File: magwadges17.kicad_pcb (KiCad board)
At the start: 2 copper layers, 156 x 89.8 mm, 44 parts, among them J1 PGM, J2 JACK_2P, U1 ATTINY861A-SU

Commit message: Update center spinner
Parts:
- removed Gsp: LOGO, custom:spiral_pattern_large4
- added REF**: Centertouch, centerspin:centerspin, F.Cu at (150.0, 100.0)
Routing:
- net TouchC: track 2.57 -> 45.0 mm
- net TouchA: track 2.39 -> 42.7 mm
- net TouchB: track 2.44 -> 9.18 mm

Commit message: Update wadges
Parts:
- moved BT1 3.30 mm to (212.1, 89.2)
- moved J2 1.56 mm to (83.5, 97.2)
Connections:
- J1 pad 3: Net-(J1-Pad3) -> SW_F
- LS1 pad 2: Net-(J1-Pad3) -> Net-(LS1-Pad2)
- U1 pad 3: Net-(J1-Pad3) -> SW_F
- U1 pad 4: Net-(J2-Pad2) -> SW_G
- U1 pad 7: SW_F -> Net-(LS1-Pad2)
- U1 pad 8: SW_G -> Net-(J2-Pad2)
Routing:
- net Net-(LS1-Pad2): track 0.00 -> 110.1 mm
- net Net-(J1-Pad3): track 85.9 -> 0.00 mm
- net GND: track 323.4 -> 371.3 mm
- net SW_F: track 72.9 -> 85.7 mm
- net SW_G: track 67.0 -> 75.3 mm
- net Net-(J2-Pad2): track 99.5 -> 106.3 mm
- net VCC: track 127.7 -> 134.3 mm
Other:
- board text added: "GO"
- board text added: "GOTTA"
- board text added: "MAGWEST"
- board text added: "WEST"

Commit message: Update design
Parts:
- added D1: LED, SM0805, F.Cu at (186.5, 114.9)
- added D2: LED, SM0805, F.Cu at (113.4, 115.2)
- added D3: LED, SM0805, F.Cu at (113.5, 83.6)
- added D4: LED, SM0805, F.Cu at (185.5, 83.8)
- added L1: LANYARD, Connectors:1pin, F.Cu at (149.9, 63.2)
- added RN2: 10k, NETWORK1206, F.Cu at (163.6, 133.8)
- RN1: value R_Pack04 -> 1M
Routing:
- net Net-(D1-Pad2): track 33.0 -> 184.9 mm, vias 0 -> 10
- net Net-(D3-Pad1): track 0.00 -> 81.2 mm, vias 0 -> 6
- net Net-(D3-Pad2): track 22.9 -> 102.9 mm, vias 0 -> 4
- net Net-(D4-Pad1): track 0.00 -> 62.2 mm, vias 0 -> 4
- net Net-(D2-Pad1): track 0.00 -> 61.4 mm
- net Net-(D1-Pad1): track 0.00 -> 34.6 mm
- net GND: track 371.3 -> 396.3 mm, vias 0 -> 8
- net reset: track 21.4 -> 36.4 mm, vias 0 -> 2
- added copper zone on B.Cu, net GND
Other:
- outline, holes or cut-outs redrawn
- rule pad_to_mask_clearance: 0.2 -> 0.1
- board text removed: "GO"
- board text removed: "GOTTA"
- board text removed: "MAGWEST"
- board text removed: "WEST"

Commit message: Update with halftone
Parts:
- added ?: , halftone:halftone, B.Cu at (150.0, 100.0)
- moved RN2 23.1 mm to (181.4, 119.2)
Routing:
- net Net-(D1-Pad1): track 34.6 -> 4.81 mm
- net Net-(D3-Pad1): track 81.2 -> 102.1 mm
- net Net-(D2-Pad1): track 61.4 -> 74.1 mm
- net Net-(D4-Pad1): track 62.2 -> 49.5 mm, vias 4 -> 2
- net GND: track 396.3 -> 406.1 mm, vias 8 -> 9
- net Net-(D1-Pad2): track 184.9 -> 183.4 mm
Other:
- outline, holes or cut-outs redrawn

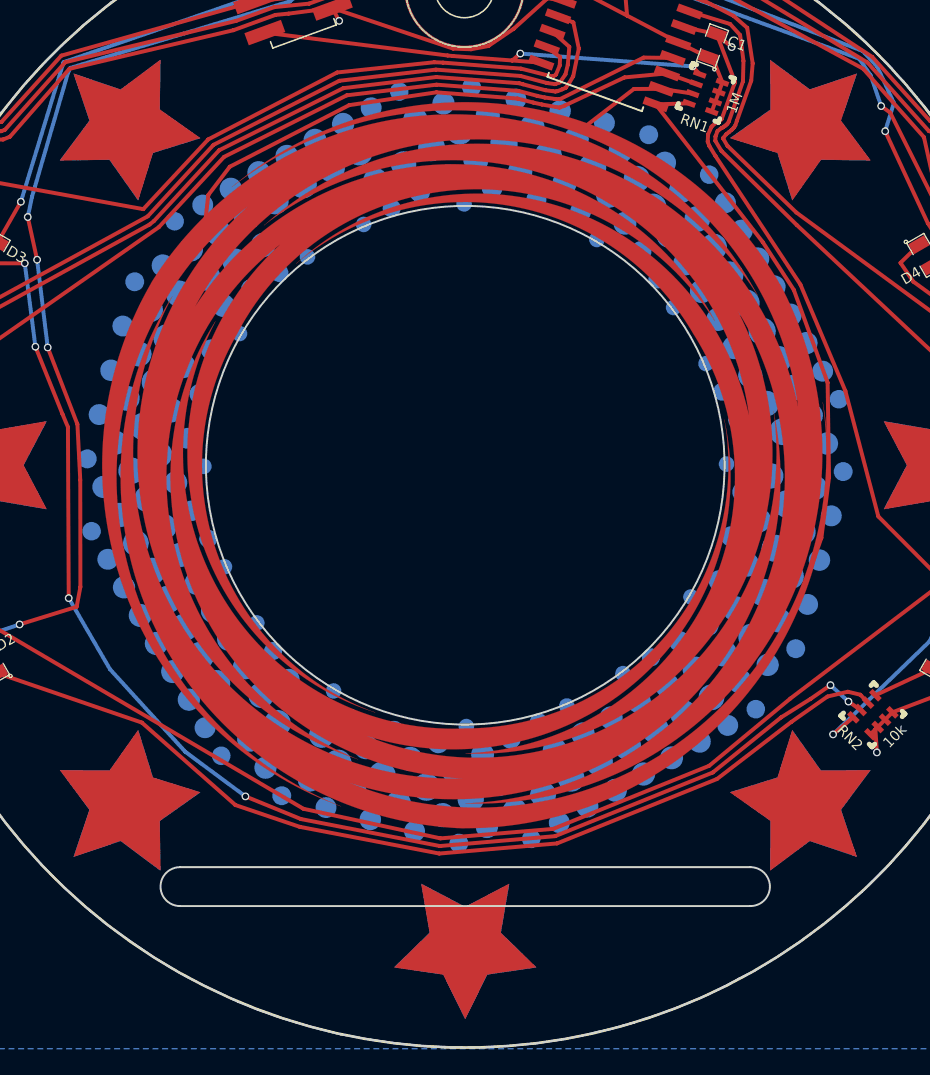
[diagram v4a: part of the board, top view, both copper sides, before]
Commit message: Update design with halftone, etc.
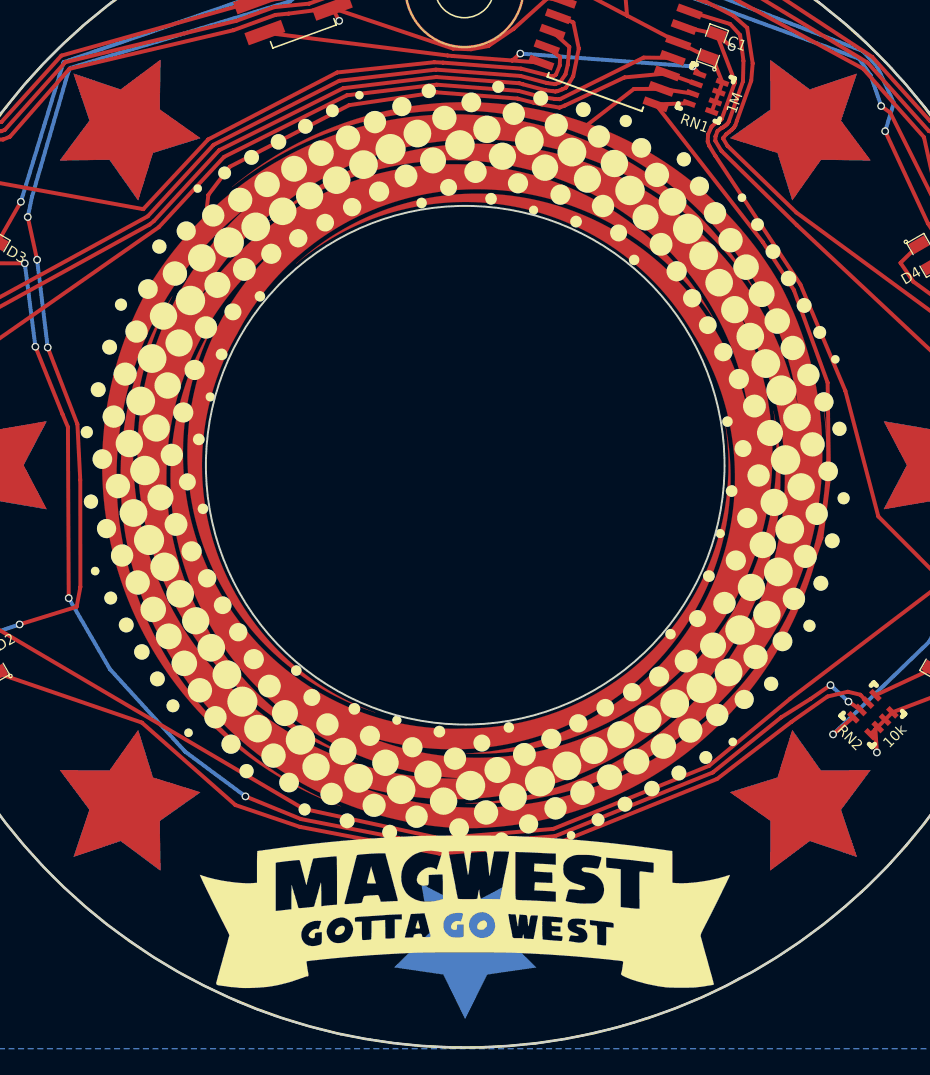
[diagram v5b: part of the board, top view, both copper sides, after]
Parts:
- removed G10, G3: LOGO, custom:test_star4
- removed G17, G24: LOGO, custom:test_star4_copper
- added ?: , halftone:halftoneSilk, F.Cu at (150.0, 100.0)
- added G***: LOGO, customs:Logo, F.Cu at (150.0, 135.5)
- added G18: LOGO, custom:test_star4_copper, B.Cu at (150.0, 137.5)
- added G4: LOGO, custom:test_star4, B.Cu at (150.0, 137.5)
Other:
- outline, holes or cut-outs redrawn

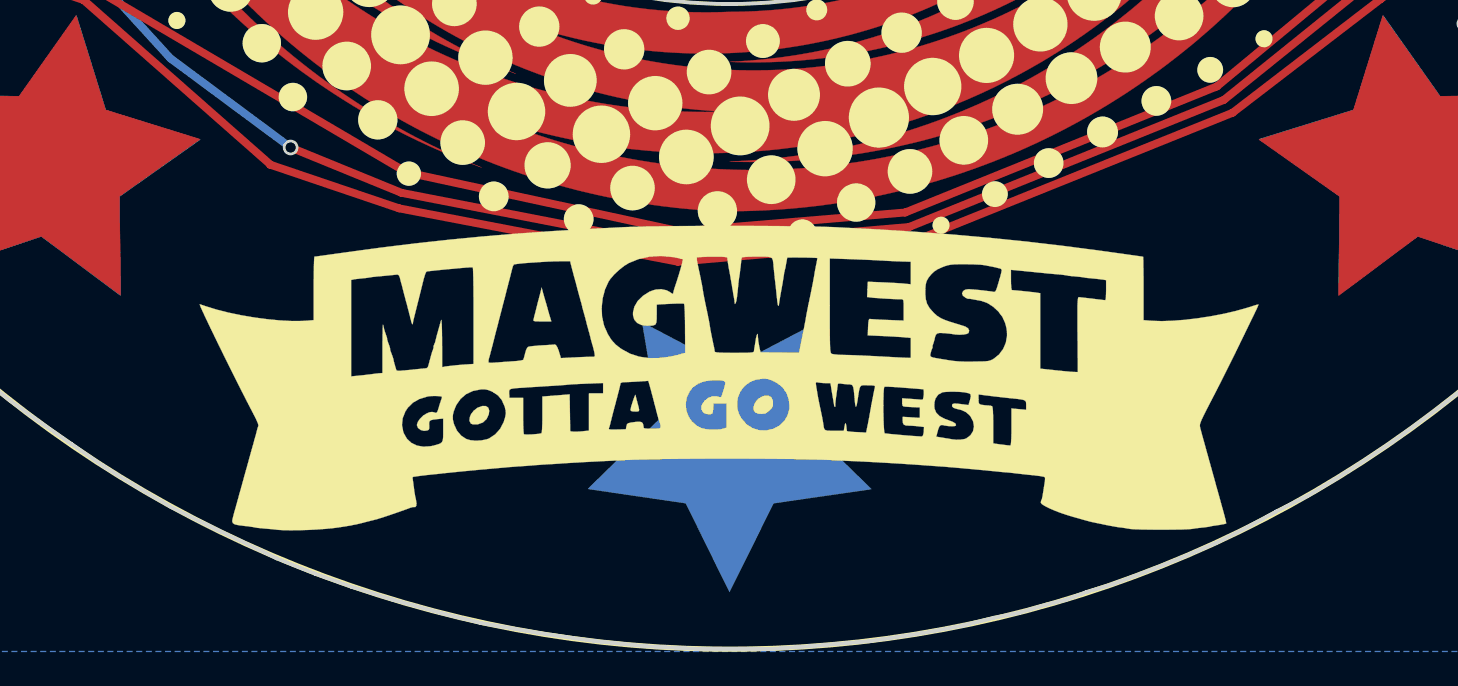
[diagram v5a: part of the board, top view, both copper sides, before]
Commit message: err apparently forgot tos ave acutal pcb
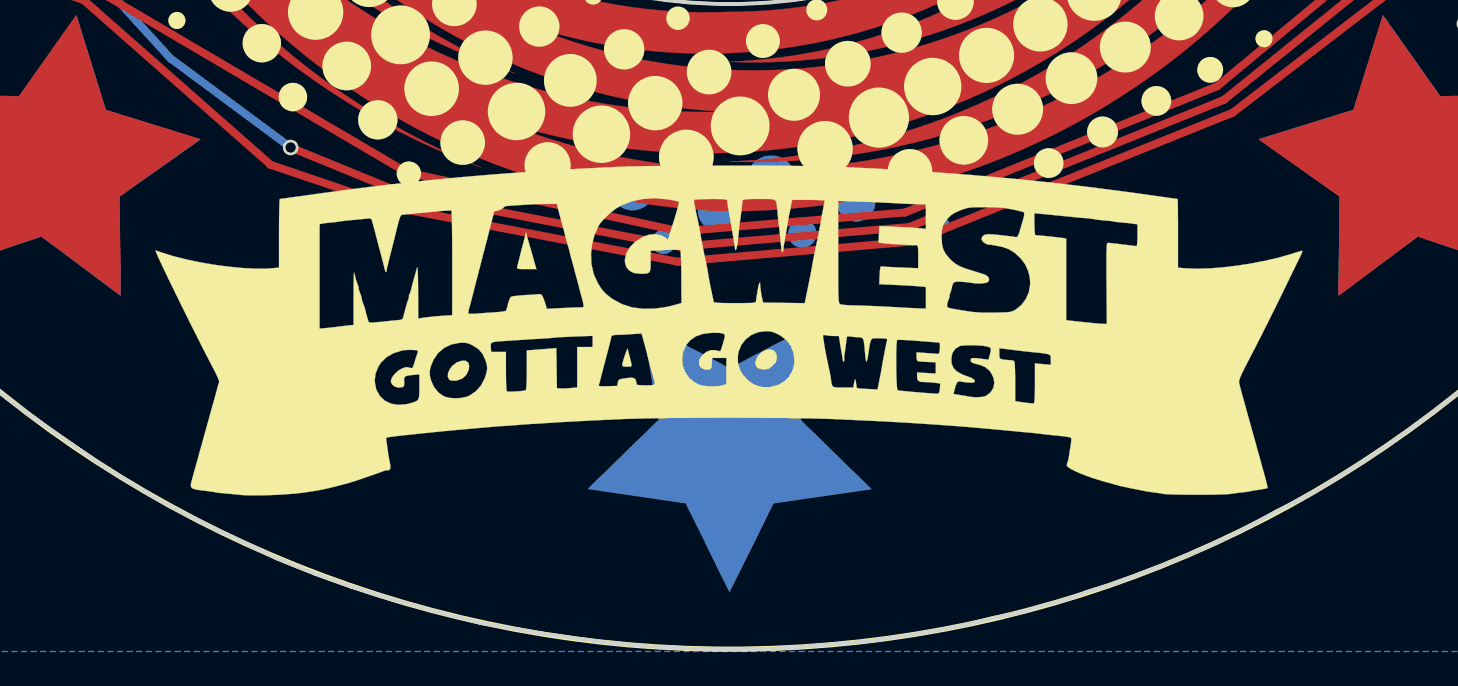
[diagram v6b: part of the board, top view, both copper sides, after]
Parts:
- moved G*** 1.75 mm to (150.0, 133.8)

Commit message: update plots rel
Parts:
- added REF**: 1Pin, SMD_Packages:1Pin, F.Cu at (150.0, 100.0)
- RN2: value 10k -> RLED
- moved BT1 2.00 mm to (214.1, 89.2), turned to 250 degrees
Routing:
- net VCC: track 134.3 -> 141.5 mm, vias 0 -> 2
- net GND: track 406.1 -> 409.1 mm
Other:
- outline, holes or cut-outs redrawn
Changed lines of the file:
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@@
-(kicad_pcb (version 4) (host pcbnew 4.0.7-e0-6372~58~ubuntu16.04.1)
+(kicad_pcb (version 4) (host pcbnew 4.0.6-e0-6349~53~ubuntu16.04.1)
   (general
     (links 55)
     (no_connects 0)
-    (area 70 54.988976 230.000001 145.011024)
+    (area 71.924999 55.024999 228.075001 144.975001)
     (thickness 1.6)
-    (drawings 194)
-    (tracks 428)
+    (drawings 193)
+    (tracks 434)
     (zones 0)
-    (modules 51)
+    (modules 52)
     (nets 23)
   )
@@
     (34 B.Paste user)
     (35 F.Paste user)
-    (36 B.SilkS user)
-    (37 F.SilkS user)
-    (38 B.Mask user)
+    (36 B.SilkS user hide)
+    (37 F.SilkS user hide)
+    (38 B.Mask user hide)
     (39 F.Mask user hide)
     (40 Dwgs.User user)
@@
     (44 Edge.Cuts user)
     (45 Margin user)
-    (46 B.CrtYd user)
-    (47 F.CrtYd user)
-    (48 B.Fab user)
-    (49 F.Fab user)
+    (46 B.CrtYd user hide)
+    (47 F.CrtYd user hide)
+    (48 B.Fab user hide)
+    (49 F.Fab user hide)
   )
   (setup
@@
     (mod_text_size 1 1)
     (mod_text_width 0.15)
-    (pad_size 9.3 9.3)
-    (pad_drill 8.9)
+    (pad_size 39.5 39.5)
+    (pad_drill 38.5)
     (pad_to_mask_clearance 0.1)
     (aux_axis_origin 0 0)
@@
   )
   (module custom:S8211-45R (layer F.Cu)
-    (at 212.14 89.19 270)
-    (fp_text reference BT1 (at 0 6.1 270) (layer F.SilkS)
+    (at 214.14 89.19 250)
+    (fp_text reference BT1 (at 0 6.1 250) (layer F.SilkS)
       (effects (font (size 1 1) (thickness 0.15)))
     )
-    (fp_text value Battery_Cell (at 0 -4.8 270) (layer F.Fab)
+    (fp_text value Battery_Cell (at 0 -4.8 250) (layer F.Fab)
       (effects (font (size 1 1) (thickness 0.15)))
     )
@@
     (fp_line (start 0.4 -9.8) (end 0 -10.3) (layer F.SilkS) (width 0.15))
     (fp_circle (center 0 0) (end 9.9 2.7) (layer F.SilkS) (width 0.15))
-    (pad 1 smd rect (at -13.45 0 270) (size 5 5.5) (layers F.Cu F.Paste F.Mask)
+    (pad 1 smd rect (at -13.45 0 250) (size 5 5.5) (layers F.Cu F.Paste F.Mask)
       (net 1 VCC))
-    (pad 2 smd rect (at 0 0 270) (size 5 5) (layers F.Cu F.Paste F.Mask)
+    (pad 2 smd circle (at 0 0 250) (size 19 19) (layers F.Cu F.Paste F.Mask)
       (net 2 GND))
-    (pad 1 smd rect (at 13.45 0 270) (size 5 5.5) (layers F.Cu F.Paste F.Mask)
+    (pad 1 smd rect (at 13.45 0 250) (size 5 5.5) (layers F.Cu F.Paste F.Mask)
       (net 1 VCC))
   )
@@
       (effects (font (size 0.8128 0.7874) (thickness 0.1524)))
     )
-    (fp_text value 10k (at -0.033 -2.356 225) (layer F.SilkS)
+    (fp_text value RLED (at -0.033 -2.356 225) (layer F.SilkS)
       (effects (font (size 0.8128 0.7874) (thickness 0.1524)))
     )
@@
       (xy -7.828776 -4.804834)) (layer F.SilkS) (width 0.01))
   )
+  (module SMD_Packages:1Pin (layer F.Cu)
+    (at 150 100)
+    (descr "module 1 pin (ou trou mecanique de percage)")
+    (tags DEV)
+    (fp_text reference REF** (at 0 -3.50012) (layer F.SilkS)
+      (effects (font (size 1 1) (thickness 0.15)))
+    )
+    (fp_text value 1Pin (at 0.24892 3.74904) (layer F.Fab)
+      (effects (font (size 1 1) (thickness 0.15)))
+    )
+    (fp_line (start -2.49936 -2.49936) (end 2.49936 -2.49936) (layer F.SilkS) (width 0.15))
+    (fp_line (start 2.49936 -2.49936) (end 2.49936 2.49936) (layer F.SilkS) (width 0.15))
+    (fp_line (start 2.49936 2.49936) (end -2.49936 2.49936) (layer F.SilkS) (width 0.15))
+    (fp_line (start -2.49936 2.49936) (end -2.49936 -2.49936) (layer F.SilkS) (width 0.15))
+    (pad 1 thru_hole circle (at 0 0) (size 39.5 39.5) (drill 38.5) (layers *.Cu *.Mask))
+  )
   (gr_circle (center 150 100) (end 149 139) (layer F.Fab) (width 0.2))
-  (gr_circle (center 150 100) (end 170 100) (layer Edge.Cuts) (width 0.15))
   (gr_circle (center 150 100) (end 194.9 100.8) (layer B.SilkS) (width 0.2))
   (gr_line (start 106 109) (end 85 109) (angle 90) (layer Edge.Cuts) (width 0.15))
@@
   (gr_arc (start 225 76) (end 225 73) (angle 90) (layer Edge.Cuts) (width 0.15))
   (gr_line (start 186 73) (end 225 73) (angle 90) (layer Edge.Cuts) (width 0.15))
-  (segment (start 212.65 76.16) (end 216.26 87.06) (width 0.3048) (layer F.Cu) (net 1))
-  (segment (start 216.26 87.06) (end 216.37 93.04) (width 0.3048) (layer F.Cu) (net 1))
-  (segment (start 216.37 93.04) (end 212.65 103.06) (width 0.3048) (layer F.Cu) (net 1))
+  (segment (start 209.539829 101.828866) (end 203.4032 96.00184) (width 0.3048) (layer F.Cu) (net 1))
+  (via (at 203.4032 96.00184) (size 0.6) (drill 0.4) (layers F.Cu B.Cu) (net 1))
+  (segment (start 203.4032 96.00184) (end 202.39736 87.1728) (width 0.3048) (layer B.Cu) (net 1))
+  (via (at 202.39736 87.1728) (size 0.6) (drill 0.4) (layers F.Cu B.Cu) (net 1))
+  (segment (start 202.39736 87.1728) (end 204.690639 75.190427) (width 0.3048) (layer F.Cu) (net 1))
+  (segment (start 212.950859 75.945508) (end 218.740171 76.551134) (width 0.3048) (layer F.Cu) (net 1))
   (segment (start 161.83 57.53) (end 162.48263 65.322602) (width 0.3048) (layer F.Cu) (net 1))
   (segment (start 158.030627 62.985801) (end 162.48263 65.322602) (width 0.3048) (layer F.Cu) (net 1))
@@
   (segment (start 145.57 55.82) (end 151.779768 55.633018) (width 0.3048) (layer F.Cu) (net 1))
   (segment (start 151.779768 55.633018) (end 151.88 55.63) (width 0.3048) (layer F.Cu) (net 1))
-  (segment (start 213 75.95) (end 185.87 73.47) (width 0.3048) (layer F.Cu) (net 1))
+  (segment (start 213 75.95) (end 212.950859 75.945508) (width 0.3048) (layer F.Cu) (net 1))
+  (segment (start 212.950859 75.945508) (end 204.690639 75.190427) (width 0.3048) (layer F.Cu) (net 1))
+  (segment (start 204.690639 75.190427) (end 185.87 73.47) (width 0.3048) (layer F.Cu) (net 1))
   (segment (start 185.87 73.47) (end 181.39 68.51) (width 0.3048) (layer F.Cu) (net 1))
   (segment (start 181.39 68.51) (end 170.42 61.3) (width 0.3048) (layer F.Cu) (net 1))
+  (segment (start 214.14 89.19) (end 201.83856 91.39174) (width 0.3048) (layer F.Cu) (net 2))
+  (segment (start 201.83856 91.39174) (end 194.414093 91.528219) (width 0.3048) (layer F.Cu) (net 2))
+  (segment (start 216.26 87.06) (end 216.37 93.04) (width 0.3048) (layer F.Cu) (net 2))
   (segment (start 137.53 126.5) (end 148.09 128.78) (width 0.3048) (layer F.Cu) (net 2))
   (segment (start 148.09 128.78) (end 156.78 128.05) (width 0.3048) (layer F.Cu) (net 2))
@@
   (via (at 86.41 100.66) (size 0.6) (drill 0.4) (layers F.Cu B.Cu) (net 2))
   (segment (start 86.41 100.66) (end 86.41 100.62) (width 0.3048) (layer B.Cu) (net 2))
-  (segment (start 212.14 89.19) (end 208.99 87.94) (width 0.3048) (layer F.Cu) (net 2))
   (via (at 208.99 87.94) (size 0.6) (drill 0.4) (layers F.Cu B.Cu) (net 2))
   (segment (start 208.99 87.94) (end 209.01 87.82) (width 0.3048) (layer B.Cu) (net 2))
@@
   (segment (start 99.0275 88.95) (end 101 85.8) (width 0.3048) (layer F.Cu) (net 2))
   (segment (start 101 85.8) (end 102.0275 79.95) (width 0.3048) (layer F.Cu) (net 2))
-  (segment (start 193.98561 86.855439) (end 209.72 87.28) (width 0.3048) (layer F.Cu) (net 2))
-  (segment (start 209.72 87.28) (end 212.65 89.61) (width 0.3048) (layer F.Cu) (net 2))
   (segment (start 153.74 66.34) (end 156.36 63.98) (width 0.3048) (layer F.Cu) (net 2))
   (segment (start 156.36 63.98) (end 157.596262 64.17921) (width 0.3048) (layer F.Cu) (net 2))
@@
   (segment (start 195.37 102.32) (end 195.27 103.96) (width 0.3048) (layer F.Cu) (net 2))
   (segment (start 195.27 103.96) (end 194.0275 106.95) (width 0.3048) (layer F.Cu) (net 2))
-  (segment (start 193.0275 88.95) (end 195.41 93.38) (width 0.3048) (layer F.Cu) (net 2))
+  (segment (start 193.0275 88.95) (end 194.414093 91.528219) (width 0.3048) (layer F.Cu) (net 2))
+  (segment (start 194.414093 91.528219) (end 195.41 93.38) (width 0.3048) (layer F.Cu) (net 2))
   (segment (start 195.41 93.38) (end 195.41 95.17) (width 0.3048) (layer F.Cu) (net 2))
   (segment (start 195.41 95.17) (end 194.0555 98) (width 0.3048) (layer F.Cu) (net 2))

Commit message: final plots as they were sent.
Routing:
- net (no net): track 0.00 -> 6.50 mm
